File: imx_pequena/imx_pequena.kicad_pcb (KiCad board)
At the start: 2 copper layers, 2 parts, among them U1 MCIMX6Z0DVM09AB, U2 MT41K64M16TW-107:J_TR

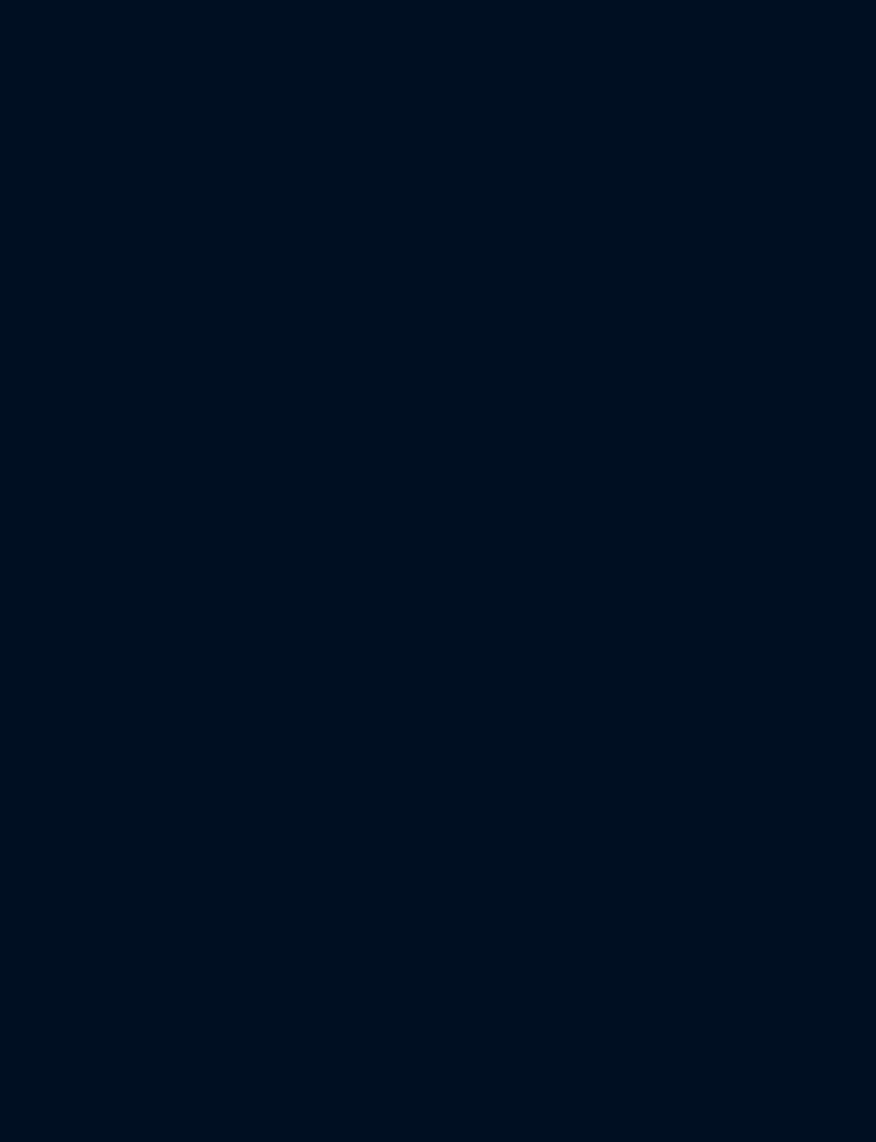
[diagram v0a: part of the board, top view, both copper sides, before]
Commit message: Updated reset pins
Updated reset pins
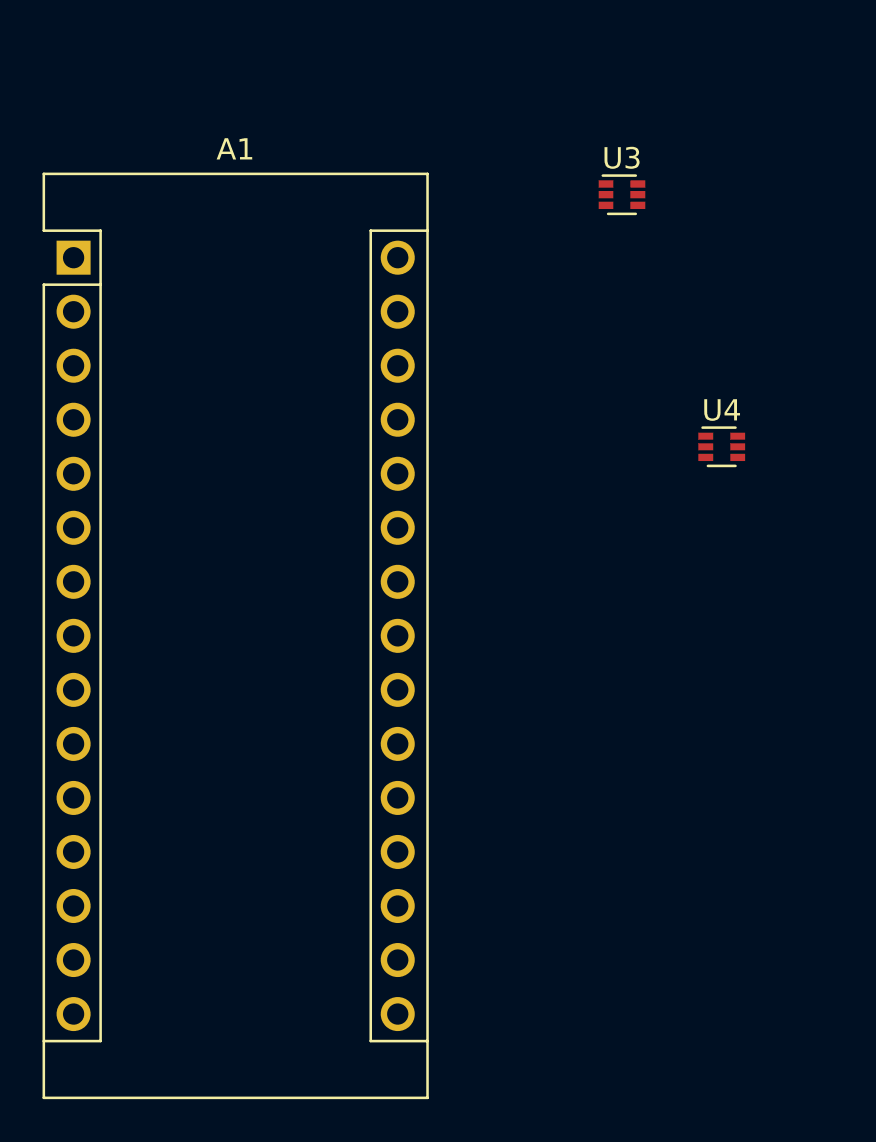
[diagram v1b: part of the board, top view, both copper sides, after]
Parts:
- added A1: Arduino_Nano_Every, Module:Arduino_Nano, F.Cu at (78.8, 100.3)
- added U3: AP62250Z6, Package_TO_SOT_SMD:SOT-563, F.Cu at (104.5, 97.4)
- added U4: AP62250Z6, Package_TO_SOT_SMD:SOT-563, F.Cu at (109.2, 109.2)
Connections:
- U1 pad A2: unconnected-(U1-PadA2) -> /imx_mpu/mpu_f_sd/SD_DATA3
- U1 pad B1: unconnected-(U1-PadB1) -> /imx_mpu/mpu_f_sd/SD_DATA2
- U1 pad B2: unconnected-(U1-PadB2) -> /imx_mpu/mpu_f_sd/SD_DATA1
- U1 pad B3: unconnected-(U1-PadB3) -> /imx_mpu/mpu_f_sd/SD_DATA0
- U1 pad C1: unconnected-(U1-PadC1) -> /imx_mpu/mpu_f_sd/SD_CLK
- U1 pad C2: unconnected-(U1-PadC2) -> /imx_mpu/mpu_f_sd/SD_CMD
- U1 pad C4: unconnected-(U1-PadC4) -> DCDC_3v3
- U1 pad F17: unconnected-(U1-PadF17) -> /imx_mpu/I2C2_SCL
- U1 pad F4: unconnected-(U1-PadF4) -> DCDC_3v3
- U1 pad G13: unconnected-(U1-PadG13) -> /imx_mpu/I2C2_SDA
- U1 pad G2: unconnected-(U1-PadG2) -> Net-(U1-PadG2)
- U1 pad G4: unconnected-(U1-PadG4) -> /imx_mpu/mpu_b_dram/DRAM_RESET
- U1 pad G6: Net-(U1-PadG6) -> Dram_1V35
- U1 pad H1: unconnected-(U1-PadH1) -> /imx_mpu/mpu_b_dram/DRAM_BA1
- U1 pad H13: unconnected-(U1-PadH13) -> Net-(U1-PadH13)
- U1 pad H2: unconnected-(U1-PadH2) -> Net-(U1-PadH2)
- U1 pad H4: unconnected-(U1-PadH4) -> Net-(U1-PadH4)
- U1 pad H6: Net-(U1-PadG6) -> Dram_1V35
- U1 pad J1: unconnected-(U1-PadJ1) -> /imx_mpu/mpu_b_dram/DRAM_WE
- U1 pad J2: unconnected-(U1-PadJ2) -> /imx_mpu/mpu_b_dram/DRAM_CAS
- U1 pad J4: unconnected-(U1-PadJ4) -> Net-(U1-PadJ4)
- U1 pad J6: Net-(U1-PadG6) -> Dram_1V35
- U1 pad K1: unconnected-(U1-PadK1) -> Net-(U1-PadK1)
- U1 pad K2: unconnected-(U1-PadK2) -> /imx_mpu/mpu_b_dram/DRAM_BA2
- U1 pad K3: unconnected-(U1-PadK3) -> Net-(U1-PadK3)
- U1 pad K4: unconnected-(U1-PadK4) -> Net-(U1-PadK4)
- U1 pad K6: Net-(U1-PadG6) -> Dram_1V35
- U1 pad L1: unconnected-(U1-PadL1) -> Net-(U1-PadL1)
- U1 pad L2: unconnected-(U1-PadL2) -> Net-(U1-PadL2)
- U1 pad L4: unconnected-(U1-PadL4) -> Net-(U1-PadL4)
- U1 pad L5: unconnected-(U1-PadL5) -> Net-(U1-PadL5)
- U1 pad L6: Net-(U1-PadG6) -> Dram_1V35
- U1 pad M1: unconnected-(U1-PadM1) -> /imx_mpu/mpu_b_dram/DRAM_BA0
- U1 pad M12: unconnected-(U1-PadM12) -> GND
- U1 pad M14: unconnected-(U1-PadM14) -> /imx_mpu/mpu_a_io/TCK
- U1 pad M2: unconnected-(U1-PadM2) -> Net-(U1-PadM2)
- U1 pad M3: unconnected-(U1-PadM3) -> /imx_mpu/mpu_b_dram/DRAM_CKE
- U1 pad M4: unconnected-(U1-PadM4) -> Net-(U1-PadM4)
- U1 pad M5: unconnected-(U1-PadM5) -> /imx_mpu/mpu_b_dram/DRAM_RAS
- U1 pad M6: Net-(U1-PadG6) -> Dram_1V35
- U1 pad N1: unconnected-(U1-PadN1) -> /imx_mpu/mpu_b_dram/DRAM_ODT
- U1 pad N14: unconnected-(U1-PadN14) -> /imx_mpu/mpu_a_io/JTAG_RESET
- U1 pad N15: unconnected-(U1-PadN15) -> /imx_mpu/mpu_a_io/TDO
- U1 pad N16: unconnected-(U1-PadN16) -> /imx_mpu/mpu_a_io/TDI
- U1 pad N2: unconnected-(U1-PadN2) -> /imx_mpu/mpu_b_dram/DRAM_CS0
- U1 pad N4: unconnected-(U1-PadN4) -> Net-(U1-PadN4)
- U1 pad N6: unconnected-(U1-PadN6) -> VDD_HIGH_CAP
- U1 pad P1: unconnected-(U1-PadP1) -> /imx_mpu/mpu_b_dram/DRAM_SDCLK0_P
- U1 pad P14: unconnected-(U1-PadP14) -> /imx_mpu/mpu_a_io/TMS
- U1 pad P2: unconnected-(U1-PadP2) -> /imx_mpu/mpu_b_dram/DRAM_SDCLK0_N
- U1 pad P4: unconnected-(U1-PadP4) -> /imx_mpu/mpu_b_dram/Dram_vref
- U1 pad P6: unconnected-(U1-PadP6) -> /imx_mpu/mpu_b_dram/DRAM_SDQS0_P
- U1 pad P7: unconnected-(U1-PadP7) -> /imx_mpu/mpu_b_dram/DRAM_SDQS0_N
- U1 pad T1: unconnected-(U1-PadT1) -> /imx_mpu/mpu_b_dram/DRAM_SDQS1_P
- U1 pad T11: unconnected-(U1-PadT11) -> Net-(U1-PadT11)
- U1 pad T12: unconnected-(U1-PadT12) -> /imx_mpu/USB1_VBUS
- U1 pad T13: unconnected-(U1-PadT13) -> /imx_mpu/USB2_DN
- U1 pad T15: unconnected-(U1-PadT15) -> /imx_mpu/USB1_DN
- U1 pad T16: unconnected-(U1-PadT16) -> Net-(U1-PadT16)
- U1 pad T17: unconnected-(U1-PadT17) -> Net-(U1-PadT17)
- U1 pad T2: unconnected-(U1-PadT2) -> /imx_mpu/mpu_b_dram/DRAM_SDQS1_N
- U1 pad T3: unconnected-(U1-PadT3) -> /imx_mpu/mpu_b_dram/DRAM_UDM
- U1 pad T7: unconnected-(U1-PadT7) -> /imx_mpu/mpu_b_dram/DRAM_LDM
- U1 pad U11: unconnected-(U1-PadU11) -> Net-(U1-PadU11)
- U1 pad U12: unconnected-(U1-PadU12) -> /imx_mpu/USB2_VBUS
- U1 pad U13: unconnected-(U1-PadU13) -> /imx_mpu/USB2_DP
- U1 pad U15: unconnected-(U1-PadU15) -> /imx_mpu/USB1_DP
- U1 pad U16: unconnected-(U1-PadU16) -> /imx_mpu/USB1_CHARGE_DETECT
- U2 pad A1: Net-(U2-PadA1) -> Dram_1V35
- U2 pad A8: Net-(U2-PadA1) -> Dram_1V35
- U2 pad A9: Net-(U2-PadA9) -> GND
- U2 pad B1: Net-(U2-PadB1) -> GND
- U2 pad B2: Net-(U2-PadB2) -> Dram_1V35
- U2 pad B3: Net-(U2-PadA9) -> GND
- U2 pad B7: unconnected-(U2-PadB7) -> /imx_mpu/mpu_b_dram/DRAM_SDQS1_N
- U2 pad B9: Net-(U2-PadB1) -> GND
- U2 pad C1: Net-(U2-PadA1) -> Dram_1V35
- U2 pad C7: unconnected-(U2-PadC7) -> /imx_mpu/mpu_b_dram/DRAM_SDQS1_P
- U2 pad C9: Net-(U2-PadA1) -> Dram_1V35
- U2 pad D1: Net-(U2-PadB1) -> GND
- U2 pad D2: Net-(U2-PadA1) -> Dram_1V35
- U2 pad D3: unconnected-(U2-PadD3) -> /imx_mpu/mpu_b_dram/DRAM_UDM
- U2 pad D8: Net-(U2-PadB1) -> GND
- U2 pad D9: Net-(U2-PadB2) -> Dram_1V35
- U2 pad E1: Net-(U2-PadA9) -> GND
- U2 pad E2: Net-(U2-PadB1) -> GND
- U2 pad E7: unconnected-(U2-PadE7) -> /imx_mpu/mpu_b_dram/DRAM_LDM
- U2 pad E8: Net-(U2-PadB1) -> GND
- U2 pad E9: Net-(U2-PadA1) -> Dram_1V35
- U2 pad F1: Net-(U2-PadA1) -> Dram_1V35
- U2 pad F3: unconnected-(U2-PadF3) -> /imx_mpu/mpu_b_dram/DRAM_SDQS0_P
- U2 pad F9: Net-(U2-PadB1) -> GND
- U2 pad G1: Net-(U2-PadB1) -> GND
- U2 pad G3: unconnected-(U2-PadG3) -> /imx_mpu/mpu_b_dram/DRAM_SDQS0_N
- U2 pad G7: Net-(U2-PadB2) -> Dram_1V35
- U2 pad G8: Net-(U2-PadA9) -> GND
- U2 pad G9: Net-(U2-PadB1) -> GND
- U2 pad H1: unconnected-(U2-PadH1) -> /imx_mpu/mpu_b_dram/Dram_vref
- U2 pad H2: Net-(U2-PadA1) -> Dram_1V35
- U2 pad H9: Net-(U2-PadA1) -> Dram_1V35
- U2 pad J2: Net-(U2-PadA9) -> GND
- U2 pad J3: unconnected-(U2-PadJ3) -> /imx_mpu/mpu_b_dram/DRAM_RAS
- U2 pad J7: unconnected-(U2-PadJ7) -> /imx_mpu/mpu_b_dram/DRAM_SDCLK0_P
- U2 pad J8: Net-(U2-PadA9) -> GND
- U2 pad K1: unconnected-(U2-PadK1) -> /imx_mpu/mpu_b_dram/DRAM_ODT
- U2 pad K2: Net-(U2-PadB2) -> Dram_1V35
- U2 pad K3: unconnected-(U2-PadK3) -> /imx_mpu/mpu_b_dram/DRAM_CAS
- U2 pad K7: unconnected-(U2-PadK7) -> /imx_mpu/mpu_b_dram/DRAM_SDCLK0_N
- U2 pad K8: Net-(U2-PadB2) -> Dram_1V35
- U2 pad K9: unconnected-(U2-PadK9) -> /imx_mpu/mpu_b_dram/DRAM_CKE
- U2 pad L2: unconnected-(U2-PadL2) -> /imx_mpu/mpu_b_dram/DRAM_CS0
- U2 pad L3: unconnected-(U2-PadL3) -> /imx_mpu/mpu_b_dram/DRAM_WE
- U2 pad L7: unconnected-(U2-PadL7) -> Net-(U1-PadM4)
- U2 pad L8: unconnected-(U2-PadL8) -> Net-(U2-PadL8)
- U2 pad M1: Net-(U2-PadA9) -> GND
- U2 pad M2: unconnected-(U2-PadM2) -> /imx_mpu/mpu_b_dram/DRAM_BA0
- U2 pad M3: unconnected-(U2-PadM3) -> /imx_mpu/mpu_b_dram/DRAM_BA2
- U2 pad M8: unconnected-(U2-PadM8) -> /imx_mpu/mpu_b_dram/Dram_vref
- U2 pad M9: Net-(U2-PadA9) -> GND
- U2 pad N1: Net-(U2-PadB2) -> Dram_1V35
- U2 pad N2: unconnected-(U2-PadN2) -> Net-(U1-PadM2)
- U2 pad N3: unconnected-(U2-PadN3) -> Net-(U1-PadL5)
- U2 pad N7: unconnected-(U2-PadN7) -> Net-(U1-PadL4)
- U2 pad N8: unconnected-(U2-PadN8) -> /imx_mpu/mpu_b_dram/DRAM_BA1
- U2 pad N9: Net-(U2-PadB2) -> Dram_1V35
- U2 pad P1: Net-(U2-PadA9) -> GND
- U2 pad P2: unconnected-(U2-PadP2) -> Net-(U1-PadL1)
- U2 pad P3: unconnected-(U2-PadP3) -> Net-(U1-PadK1)
- U2 pad P7: unconnected-(U2-PadP7) -> Net-(U1-PadH2)
- U2 pad P8: unconnected-(U2-PadP8) -> Net-(U1-PadK4)
- U2 pad P9: Net-(U2-PadA9) -> GND
- U2 pad R1: Net-(U2-PadB2) -> Dram_1V35
- U2 pad R2: unconnected-(U2-PadR2) -> Net-(U1-PadH4)
- U2 pad R3: unconnected-(U2-PadR3) -> Net-(U1-PadL2)
- U2 pad R7: unconnected-(U2-PadR7) -> Net-(U1-PadK3)
- U2 pad R8: unconnected-(U2-PadR8) -> Net-(U1-PadG2)
- U2 pad R9: Net-(U2-PadB2) -> Dram_1V35
- U2 pad T1: Net-(U2-PadA9) -> GND
- U2 pad T2: unconnected-(U2-PadT2) -> /imx_mpu/mpu_b_dram/DRAM_RESET
- U2 pad T8: unconnected-(U2-PadT8) -> Net-(U1-PadJ4)
- U2 pad T9: Net-(U2-PadA9) -> GND

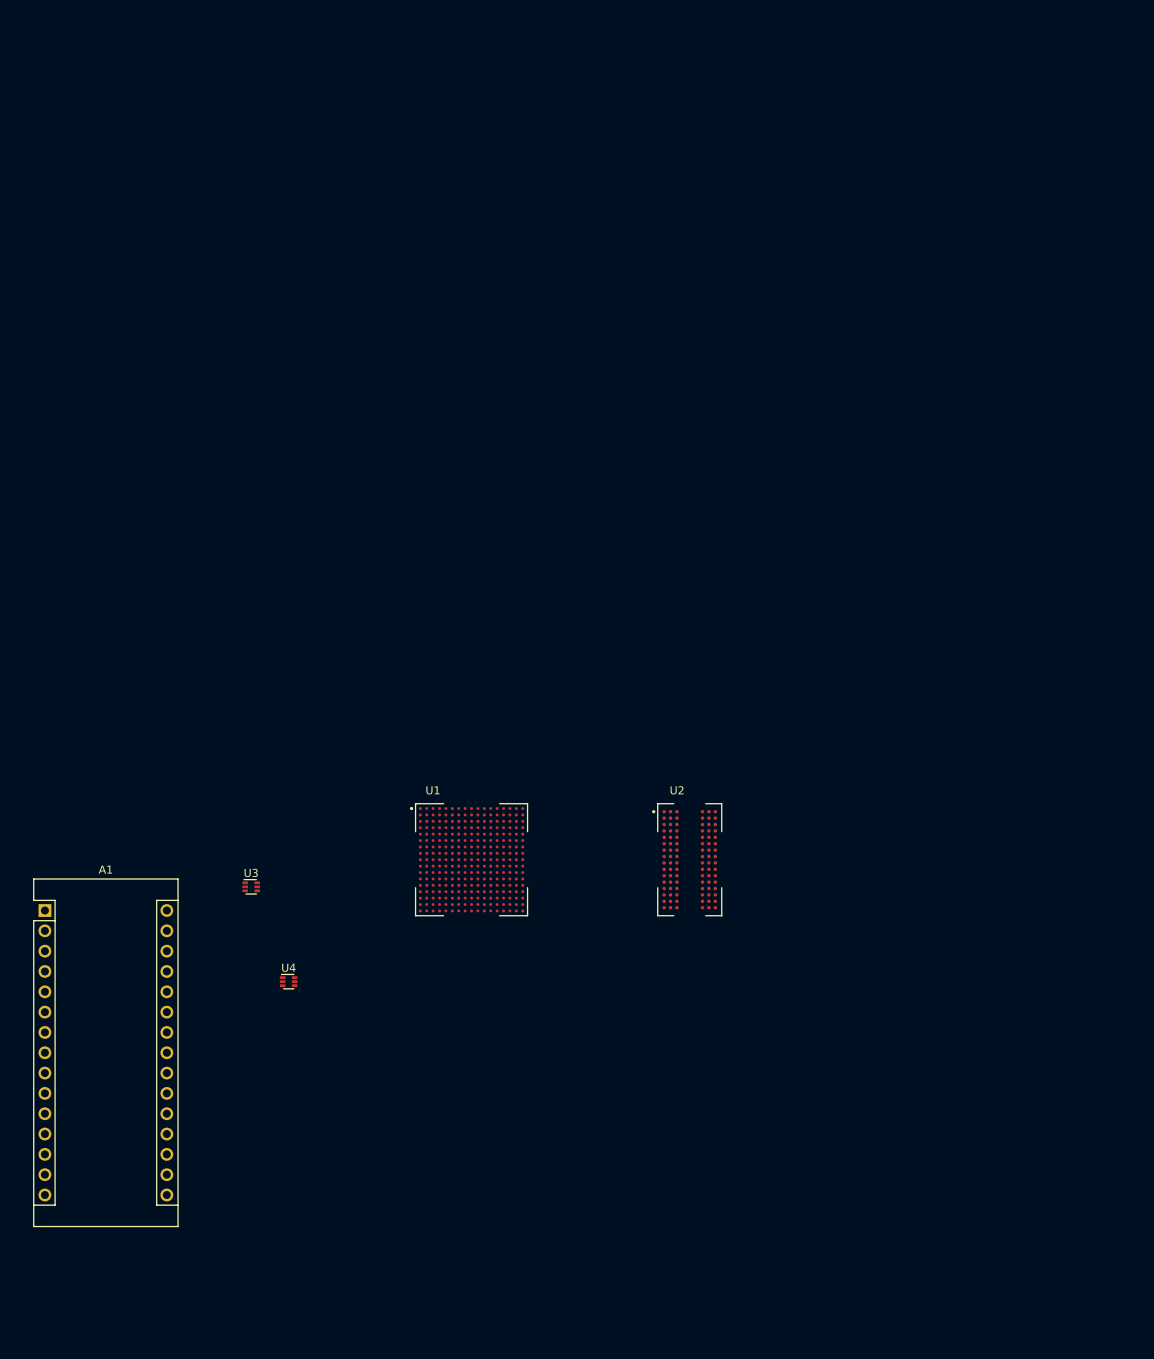
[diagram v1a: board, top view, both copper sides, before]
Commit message: Part Assignment
Assigned GPIOs and assigned footprints to most parts
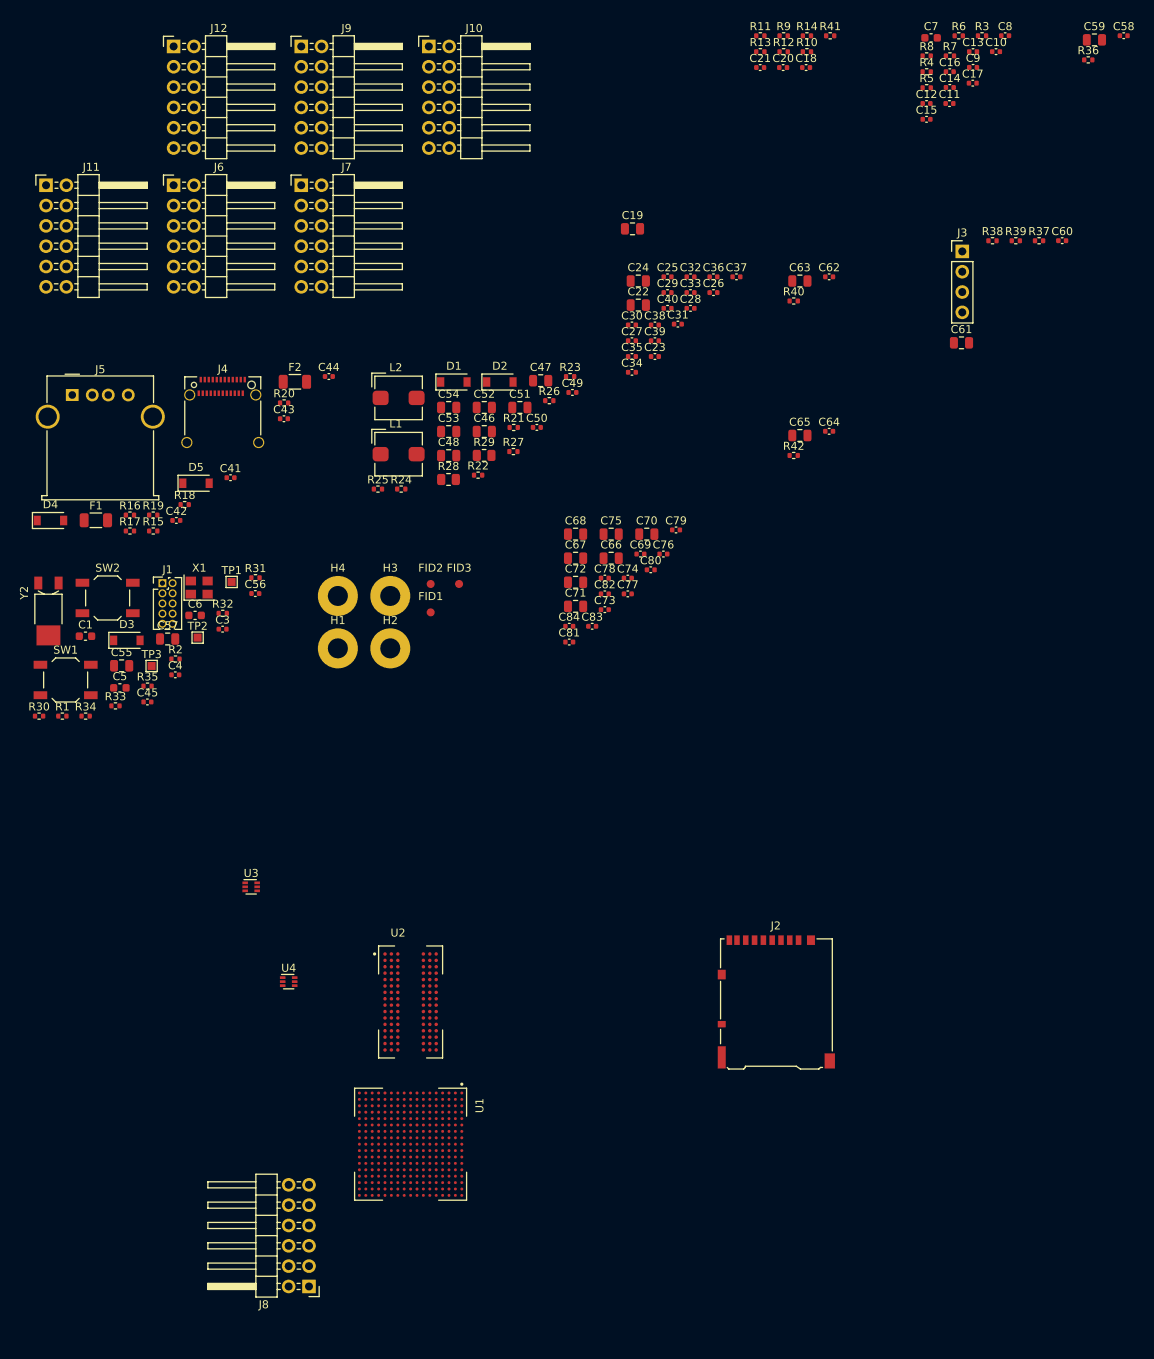
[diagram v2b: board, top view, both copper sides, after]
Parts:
- removed A1: Arduino_Nano_Every, Module:Arduino_Nano
- added C1: 1u, Capacitor_SMD:C_0603_1608Metric, F.Cu at (83.8, 66.0)
- added C10: 0.22u, Capacitor_SMD:C_0402_1005Metric, F.Cu at (197.6, -7.03)
- added C11: 0.22u, Capacitor_SMD:C_0402_1005Metric, F.Cu at (191.8, -0.54)
- added C12: 0.22u, Capacitor_SMD:C_0402_1005Metric, F.Cu at (188.9, -0.54)
- added C13: 0.22u, Capacitor_SMD:C_0402_1005Metric, F.Cu at (194.8, -7.03)
- added C14: DNP, Capacitor_SMD:C_0402_1005Metric, F.Cu at (191.9, -2.55)
- added C15: DNP, Capacitor_SMD:C_0402_1005Metric, F.Cu at (188.9, 1.43)
- added C16: 2.2p, Capacitor_SMD:C_0402_1005Metric, F.Cu at (191.9, -4.52)
- added C17: 2.2p, Capacitor_SMD:C_0402_1005Metric, F.Cu at (194.7, -3.09)
- added C18: 0.1u, Capacitor_SMD:C_0402_1005Metric, F.Cu at (173.9, -5.04)
- added C19: 22u, Capacitor_SMD:C_0805_2012Metric, F.Cu at (152.2, 15.1)
- added C20: 0.22u, Capacitor_SMD:C_0402_1005Metric, F.Cu at (171.0, -5.04)
- added C21: 0.22u, Capacitor_SMD:C_0402_1005Metric, F.Cu at (168.2, -5.04)
- added C22: 22u, Capacitor_SMD:C_0805_2012Metric, F.Cu at (152.9, 24.6)
- added C23: 0.22u, Capacitor_SMD:C_0402_1005Metric, F.Cu at (155.0, 31.1)
- added C24: 10u, Capacitor_SMD:C_0805_2012Metric, F.Cu at (152.9, 21.6)
- added C25: 0.22u, Capacitor_SMD:C_0402_1005Metric, F.Cu at (156.6, 21.1)
- added C26: 0.22u, Capacitor_SMD:C_0402_1005Metric, F.Cu at (162.3, 23.1)
- added C27: 0.22u, Capacitor_SMD:C_0402_1005Metric, F.Cu at (152.1, 29.1)
- added C28: 0.22u, Capacitor_SMD:C_0402_1005Metric, F.Cu at (159.4, 25.1)
- added C29: 0.22u, Capacitor_SMD:C_0402_1005Metric, F.Cu at (156.6, 23.1)
- added C3: 15p, Capacitor_SMD:C_0402_1005Metric, F.Cu at (101.0, 65.2)
- added C30: 0.22u, Capacitor_SMD:C_0402_1005Metric, F.Cu at (152.1, 27.1)
- added C31: 0.22u, Capacitor_SMD:C_0402_1005Metric, F.Cu at (157.9, 27.0)
- added C32: 0.22u, Capacitor_SMD:C_0402_1005Metric, F.Cu at (159.4, 21.1)
- added C33: 0.22u, Capacitor_SMD:C_0402_1005Metric, F.Cu at (159.4, 23.1)
- added C34: 0.22u, Capacitor_SMD:C_0402_1005Metric, F.Cu at (152.1, 33.0)
- added C35: 0.22u, Capacitor_SMD:C_0402_1005Metric, F.Cu at (152.1, 31.1)
- added C36: 0.22u, Capacitor_SMD:C_0402_1005Metric, F.Cu at (162.3, 21.1)
- added C37: 0.22u, Capacitor_SMD:C_0402_1005Metric, F.Cu at (165.2, 21.1)
- added C38: 0.22u, Capacitor_SMD:C_0402_1005Metric, F.Cu at (155.0, 27.1)
- added C39: 0.22u, Capacitor_SMD:C_0402_1005Metric, F.Cu at (155.0, 29.1)
- added C4: 15p, Capacitor_SMD:C_0402_1005Metric, F.Cu at (95.0, 70.9)
- added C40: 0.22u, Capacitor_SMD:C_0402_1005Metric, F.Cu at (156.6, 25.1)
- added C41: 47pF, Capacitor_SMD:C_0402_1005Metric, F.Cu at (102.0, 46.2)
- added C42: 47pF, Capacitor_SMD:C_0402_1005Metric, F.Cu at (95.2, 51.6)
- added C43: 47pF, Capacitor_SMD:C_0402_1005Metric, F.Cu at (108.6, 38.9)
- added C44: 47pF, Capacitor_SMD:C_0402_1005Metric, F.Cu at (114.2, 33.6)
- added C45: DNP, Capacitor_SMD:C_0402_1005Metric, F.Cu at (91.6, 74.3)
- added C46: 10u, Capacitor_SMD:C_0805_2012Metric, F.Cu at (133.7, 40.5)
- added C47: 10u, Capacitor_SMD:C_0805_2012Metric, F.Cu at (140.7, 34.1)
- added C48: 10n, Capacitor_SMD:C_0805_2012Metric, F.Cu at (129.2, 43.5)
- added C49: 100n, Capacitor_SMD:C_0402_1005Metric, F.Cu at (144.7, 35.6)
- added C5: 1u, Capacitor_SMD:C_0603_1608Metric, F.Cu at (88.1, 72.5)
- added C50: 100n, Capacitor_SMD:C_0402_1005Metric, F.Cu at (140.2, 39.9)
- added C51: 22u, Capacitor_SMD:C_0805_2012Metric, F.Cu at (138.1, 37.5)
- added C52: 22u, Capacitor_SMD:C_0805_2012Metric, F.Cu at (133.7, 37.5)
- added C53: 22u, Capacitor_SMD:C_0805_2012Metric, F.Cu at (129.2, 40.5)
- added C54: 22u, Capacitor_SMD:C_0805_2012Metric, F.Cu at (129.2, 37.5)
- added C55: DNP, Capacitor_SMD:C_0805_2012Metric, F.Cu at (88.3, 69.7)
- added C56: 0.22uF, Capacitor_SMD:C_0402_1005Metric, F.Cu at (105.0, 60.7)
- added C57: 10u, Capacitor_SMD:C_0805_2012Metric, F.Cu at (94.1, 66.4)
- added C58: 0.22uF, Capacitor_SMD:C_0402_1005Metric, F.Cu at (213.6, -9.02)
- added C59: 10u, Capacitor_SMD:C_0805_2012Metric, F.Cu at (209.9, -8.50)
- added C6: 1u, Capacitor_SMD:C_0603_1608Metric, F.Cu at (97.5, 63.4)
- added C60: 0.22uF, Capacitor_SMD:C_0402_1005Metric, F.Cu at (205.9, 16.6)
- added C61: 10u, Capacitor_SMD:C_0805_2012Metric, F.Cu at (193.3, 29.4)
- added C62: 0.22uF, Capacitor_SMD:C_0402_1005Metric, F.Cu at (176.8, 21.1)
- added C63: 10u, Capacitor_SMD:C_0805_2012Metric, F.Cu at (173.1, 21.6)
- added C64: 0.22uF, Capacitor_SMD:C_0402_1005Metric, F.Cu at (176.8, 40.4)
- added C65: 10u, Capacitor_SMD:C_0805_2012Metric, F.Cu at (173.1, 41.0)
- added C66: 22u, Capacitor_SMD:C_0805_2012Metric, F.Cu at (149.5, 56.3)
- added C67: 22u, Capacitor_SMD:C_0805_2012Metric, F.Cu at (145.1, 56.3)
- added C68: 4.7u, Capacitor_SMD:C_0805_2012Metric, F.Cu at (145.1, 53.3)
- added C69: 0.22u, Capacitor_SMD:C_0402_1005Metric, F.Cu at (153.2, 55.8)
- added C7: 4.7u, Capacitor_SMD:C_0603_1608Metric, F.Cu at (189.5, -8.75)
- added C70: 22u, Capacitor_SMD:C_0805_2012Metric, F.Cu at (154.0, 53.3)
- added C71: 22u, Capacitor_SMD:C_0805_2012Metric, F.Cu at (145.1, 62.3)
- added C72: 10u, Capacitor_SMD:C_0805_2012Metric, F.Cu at (145.1, 59.3)
- added C73: 0.22u, Capacitor_SMD:C_0402_1005Metric, F.Cu at (148.7, 62.7)
- added C74: 0.22u, Capacitor_SMD:C_0402_1005Metric, F.Cu at (151.6, 58.8)
- added C75: 4.7u, Capacitor_SMD:C_0805_2012Metric, F.Cu at (149.5, 53.3)
- added C76: 0.22u, Capacitor_SMD:C_0402_1005Metric, F.Cu at (156.1, 55.8)
- added C77: 0.22u, Capacitor_SMD:C_0402_1005Metric, F.Cu at (151.6, 60.8)
- added C78: 0.22u, Capacitor_SMD:C_0402_1005Metric, F.Cu at (148.7, 58.8)
- added C79: 0.22u, Capacitor_SMD:C_0402_1005Metric, F.Cu at (157.6, 52.8)
- added C8: 0.1u, Capacitor_SMD:C_0402_1005Metric, F.Cu at (198.8, -9.02)
- added C80: 0.22u, Capacitor_SMD:C_0402_1005Metric, F.Cu at (154.5, 57.7)
- added C81: 0.22u, Capacitor_SMD:C_0402_1005Metric, F.Cu at (144.3, 66.8)
- added C82: 0.22u, Capacitor_SMD:C_0402_1005Metric, F.Cu at (148.7, 60.8)
- added C83: 0.22u, Capacitor_SMD:C_0402_1005Metric, F.Cu at (147.2, 64.8)
- added C84: 0.22u, Capacitor_SMD:C_0402_1005Metric, F.Cu at (144.3, 64.8)
- added C9: 0.1u, Capacitor_SMD:C_0402_1005Metric, F.Cu at (194.8, -5.06)
- added D1: D_Zener, Diode_SMD:D_SOD-123, F.Cu at (129.9, 34.3)
- added D2: D_Schottky, Diode_SMD:D_SOD-123, F.Cu at (135.6, 34.3)
- added D3: D_Schottky, Diode_SMD:D_SOD-123, F.Cu at (89.0, 66.6)
- added D4: D_TVS, Diode_SMD:D_SOD-123, F.Cu at (79.4, 51.6)
- added D5: D_TVS, Diode_SMD:D_SOD-123, F.Cu at (97.6, 46.9)
- added F1: Fuse_Small, Resistor_SMD:R_1206_3216Metric, F.Cu at (85.1, 51.5)
- added F2: Fuse_Small, Resistor_SMD:R_1206_3216Metric, F.Cu at (110.0, 34.2)
- added FID1: Fiducial, Fiducial:Fiducial_1mm_Mask2mm, F.Cu at (127.0, 63.1)
- added FID2: Fiducial, Fiducial:Fiducial_1mm_Mask2mm, F.Cu at (127.0, 59.5)
- added FID3: Fiducial, Fiducial:Fiducial_1mm_Mask2mm, F.Cu at (130.5, 59.5)
- added H1: MountingHole, MountingHole:MountingHole_2.5mm_Pad, F.Cu at (115.4, 67.6)
- added H2: MountingHole, MountingHole:MountingHole_2.5mm_Pad, F.Cu at (121.9, 67.6)
- added H3: MountingHole, MountingHole:MountingHole_2.5mm_Pad, F.Cu at (121.9, 61.0)
- added H4: MountingHole_Pad, MountingHole:MountingHole_2.5mm_Pad, F.Cu at (115.4, 61.0)
- added J1: Conn_ARM_JTAG_SWD_10, Connector_PinHeader_1.27mm:PinHeader_2x05_P1.27mm_Vertical, F.Cu at (93.4, 59.4)
- added J10: Conn_02x06_Top_Bottom, Connector_PinHeader_2.54mm:PinHeader_2x06_P2.54mm_Horizontal, F.Cu at (126.7, -7.68)
- added J11: Conn_02x06_Top_Bottom, Connector_PinHeader_2.54mm:PinHeader_2x06_P2.54mm_Horizontal, F.Cu at (78.9, 9.67)
- added J12: Conn_02x06_Top_Bottom, Connector_PinHeader_2.54mm:PinHeader_2x06_P2.54mm_Horizontal, F.Cu at (94.8, -7.68)
- added J2: Micro_SD_Card, Connector_Card:microSD_HC_Hirose_DM3AT-SF-PEJM5, F.Cu at (170.2, 111.8)
- added J3: Conn_01x04, Connector_PinHeader_2.54mm:PinHeader_1x04_P2.54mm_Vertical, F.Cu at (193.4, 17.9)
- added J4: USB_C_Receptacle, Connector_USB:USB_C_Receptacle_Amphenol_12401610E4-2A_CircularHoles, F.Cu at (101.0, 39.0)
- added J5: USB_A, Connector_USB:USB_A_Molex_67643_Horizontal, F.Cu at (82.2, 35.9)
- added J6: Conn_02x06_Top_Bottom, Connector_PinHeader_2.54mm:PinHeader_2x06_P2.54mm_Horizontal, F.Cu at (94.8, 9.67)
- added J7: Conn_02x06_Top_Bottom, Connector_PinHeader_2.54mm:PinHeader_2x06_P2.54mm_Horizontal, F.Cu at (110.8, 9.67)
- added J8: Conn_02x06_Top_Bottom, Connector_PinHeader_2.54mm:PinHeader_2x06_P2.54mm_Horizontal, F.Cu at (111.8, 147.3)
- added J9: Conn_02x06_Top_Bottom, Connector_PinHeader_2.54mm:PinHeader_2x06_P2.54mm_Horizontal, F.Cu at (110.8, -7.68)
- added L1: 2.2u, Inductor_SMD:L_Bourns_SRP5030T, F.Cu at (123.0, 43.3)
- added L2: 1.0u, Inductor_SMD:L_Bourns_SRP5030T, F.Cu at (123.0, 36.3)
- added R1: 4.7K, Resistor_SMD:R_0402_1005Metric, F.Cu at (80.9, 76.0)
- added R10: 10K, Resistor_SMD:R_0402_1005Metric, F.Cu at (174.0, -7.02)
- added R11: 10K, Resistor_SMD:R_0402_1005Metric, F.Cu at (168.2, -9.01)
- added R12: 10K, Resistor_SMD:R_0402_1005Metric, F.Cu at (171.1, -7.02)
- added R13: 10K, Resistor_SMD:R_0402_1005Metric, F.Cu at (168.2, -7.02)
- added R14: 10K, Resistor_SMD:R_0402_1005Metric, F.Cu at (174.0, -9.01)
- added R15: 22, Resistor_SMD:R_0402_1005Metric, F.Cu at (92.3, 52.9)
- added R16: 22, Resistor_SMD:R_0402_1005Metric, F.Cu at (89.4, 50.9)
- added R17: 5.1K, Resistor_SMD:R_0402_1005Metric, F.Cu at (89.4, 52.9)
- added R18: 5.1K, Resistor_SMD:R_0402_1005Metric, F.Cu at (96.2, 49.6)
- added R19: 22, Resistor_SMD:R_0402_1005Metric, F.Cu at (92.3, 50.9)
- added R2: 4.7K, Resistor_SMD:R_0402_1005Metric, F.Cu at (95.1, 68.9)
- added R20: 22, Resistor_SMD:R_0402_1005Metric, F.Cu at (108.7, 36.9)
- added R21: 10K, Resistor_SMD:R_0402_1005Metric, F.Cu at (137.3, 40.0)
- added R22: 10K, Resistor_SMD:R_0402_1005Metric, F.Cu at (132.9, 45.9)
- added R23: 31.6K, Resistor_SMD:R_0402_1005Metric, F.Cu at (144.4, 33.6)
- added R24: 10K, Resistor_SMD:R_0402_1005Metric, F.Cu at (123.3, 47.6)
- added R25: 75, Resistor_SMD:R_0402_1005Metric, F.Cu at (120.4, 47.6)
- added R26: 6.8K, Resistor_SMD:R_0402_1005Metric, F.Cu at (141.8, 36.6)
- added R27: 10K, Resistor_SMD:R_0402_1005Metric, F.Cu at (137.3, 43.0)
- added R28: 0.1, Resistor_SMD:R_0805_2012Metric, F.Cu at (129.2, 46.5)
- added R29: 0.1, Resistor_SMD:R_0805_2012Metric, F.Cu at (133.7, 43.4)
- added R3: 1.5K, Resistor_SMD:R_0402_1005Metric, F.Cu at (195.9, -9.01)
- added R30: 10K, Resistor_SMD:R_0402_1005Metric, F.Cu at (78.0, 76.0)
- added R31: 10K, Resistor_SMD:R_0402_1005Metric, F.Cu at (105.1, 58.7)
- added R32: DNI, Resistor_SMD:R_0402_1005Metric, F.Cu at (101.0, 63.2)
- added R33: 0, Resistor_SMD:R_0402_1005Metric, F.Cu at (87.6, 74.8)
- added R34: 0, Resistor_SMD:R_0402_1005Metric, F.Cu at (83.8, 76.0)
- added R35: DNP, Resistor_SMD:R_0402_1005Metric, F.Cu at (91.6, 72.3)
- added R36: 0, Resistor_SMD:R_0402_1005Metric, F.Cu at (209.2, -6.00)
- added R37: 4.7K, Resistor_SMD:R_0402_1005Metric, F.Cu at (203.0, 16.6)
- added R38: 4.7K, Resistor_SMD:R_0402_1005Metric, F.Cu at (197.2, 16.6)
- added R39: 0, Resistor_SMD:R_0402_1005Metric, F.Cu at (200.1, 16.6)
- added R4: 1.5K, Resistor_SMD:R_0402_1005Metric, F.Cu at (189.0, -4.51)
- added R40: 0, Resistor_SMD:R_0402_1005Metric, F.Cu at (172.3, 24.1)
- added R41: 0, Resistor_SMD:R_0402_1005Metric, F.Cu at (176.9, -9.01)
- added R42: 0, Resistor_SMD:R_0402_1005Metric, F.Cu at (172.3, 43.5)
- added R5: 240, Resistor_SMD:R_0402_1005Metric, F.Cu at (189.0, -2.52)
- added R6: 10K, Resistor_SMD:R_0402_1005Metric, F.Cu at (193.0, -9.01)
- added R7: 240, Resistor_SMD:R_0402_1005Metric, F.Cu at (191.9, -6.50)
- added R8: 470, Resistor_SMD:R_0402_1005Metric, F.Cu at (189.0, -6.50)
- added R9: 10K, Resistor_SMD:R_0402_1005Metric, F.Cu at (171.1, -9.01)
- added SW1: SW_SPST, Button_Switch_SMD:SW_SPST_TL3342, F.Cu at (81.3, 71.5)
- added SW2: SW_SPST, Button_Switch_SMD:SW_SPST_TL3342, F.Cu at (86.6, 61.3)
- added TP1: Bootmode 0, TestPoint:TestPoint_Pad_1.0x1.0mm, F.Cu at (102.1, 59.3)
- added TP2: Bootmode 1, TestPoint:TestPoint_Pad_1.0x1.0mm, F.Cu at (97.8, 66.2)
- added TP3: SNVS, TestPoint:TestPoint_Pad_1.0x1.0mm, F.Cu at (92.1, 69.8)
- added X1: ASE-xxxMHz, Oscillator:Oscillator_SMD_Abracon_ASE-4Pin_3.2x2.5mm, F.Cu at (98.0, 60.0)
- added Y2: Crystal, Crystal:Crystal_SMD_MicroCrystal_MS1V-T1K, F.Cu at (79.2, 62.9)
- moved U2 39.2 mm to (124.5, 111.8)
- moved U1 36.4 mm to (124.5, 129.5), turned to -90 degrees
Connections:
- net DCDC_3v3 renamed /imx_mpu/mpu_f_sd/SD_3v3
- net Net-(U1-PadG10) renamed /imx_mpu/mpu_h_power/ARM_CAP
- net Net-(U1-PadG8) renamed /imx_mpu/mpu_h_power/SOC_CAP
- net Net-(U1-PadR14) renamed /imx_mpu/mpu_h_power/HIGH_CAP
- U1 pad A1: Net-(U1-PadA1) -> GND
- U1 pad A10: unconnected-(U1-PadA10) -> ecspi_ss2
- U1 pad A11: unconnected-(U1-PadA11) -> GPIO3_14
- U1 pad A12: unconnected-(U1-PadA12) -> GPIO3_19
- U1 pad A13: unconnected-(U1-PadA13) -> GPIO3_23
- U1 pad A14: unconnected-(U1-PadA14) -> ecspi_mosi
- U1 pad A17: Net-(U1-PadA1) -> GND
- U1 pad A8: unconnected-(U1-PadA8) -> GPIO3_0
- U1 pad A9: unconnected-(U1-PadA9) -> GPIO3_6
- U1 pad B10: unconnected-(U1-PadB10) -> ecspi_ss1
- U1 pad B11: unconnected-(U1-PadB11) -> GPIO3_13
- U1 pad B12: unconnected-(U1-PadB12) -> GPIO3_18
- U1 pad B13: unconnected-(U1-PadB13) -> GPIO3_22
- U1 pad B14: unconnected-(U1-PadB14) -> ecspi_ss0
- U1 pad B16: unconnected-(U1-PadB16) -> ecspi_miso
- U1 pad B8: unconnected-(U1-PadB8) -> GPIO3_1
- U1 pad B9: unconnected-(U1-PadB9) -> GPIO3_5
- U1 pad C10: unconnected-(U1-PadC10) -> GPIO3_9
- U1 pad C11: Net-(U1-PadA1) -> GND
- U1 pad C12: unconnected-(U1-PadC12) -> ecspi_rdy
- U1 pad C13: unconnected-(U1-PadC13) -> GPIO3_21
- U1 pad C14: unconnected-(U1-PadC14) -> ecspi_sclk
- U1 pad C15: Net-(U1-PadA1) -> GND
- U1 pad C3: Net-(U1-PadA1) -> GND
- U1 pad C7: Net-(U1-PadA1) -> GND
- U1 pad C9: unconnected-(U1-PadC9) -> GPIO3_3
- U1 pad D10: unconnected-(U1-PadD10) -> GPIO3_8
- U1 pad D11: unconnected-(U1-PadD11) -> ecspi_ss3
- U1 pad D12: unconnected-(U1-PadD12) -> GPIO3_16
- U1 pad D13: unconnected-(U1-PadD13) -> GPIO3_20
- U1 pad D14: unconnected-(U1-PadD14) -> GPIO3_24
- U1 pad D9: unconnected-(U1-PadD9) -> GPIO3_2
- U1 pad E10: unconnected-(U1-PadE10) -> PWM3_out
- U1 pad E11: Net-(U1-PadA1) -> GND
- U1 pad E12: unconnected-(U1-PadE12) -> GPIO3_15
- U1 pad E13: unconnected-(U1-PadE13) -> Net-(U1-PadE13)
- U1 pad E7: unconnected-(U1-PadE7) -> Net-(U1-PadE7)
- U1 pad E8: Net-(U1-PadA1) -> GND
- U1 pad E9: unconnected-(U1-PadE9) -> GPIO3_4
- U1 pad F10: Net-(U1-PadF10) -> GND
- U1 pad F11: Net-(U1-PadF10) -> GND
- U1 pad F12: Net-(U1-PadF10) -> GND
- U1 pad F13: unconnected-(U1-PadF13) -> Net-(U1-PadF13)
- U1 pad F6: Net-(U1-PadA1) -> GND
- U1 pad F7: Net-(U1-PadA1) -> GND
- U1 pad F8: Net-(U1-PadF10) -> GND
- U1 pad F9: Net-(U1-PadF10) -> GND
- U1 pad G12: Net-(U1-PadF10) -> GND
- U1 pad G15: Net-(U1-PadF10) -> GND
- U1 pad G16: unconnected-(U1-PadG16) -> /imx_mpu/I2C1_SDA
- U1 pad G17: unconnected-(U1-PadG17) -> /imx_mpu/I2C1_SCL
- U1 pad G3: Net-(U1-PadF10) -> GND
- U1 pad G5: Net-(U1-PadF10) -> GND
- U1 pad G7: Net-(U1-PadF10) -> GND
- U1 pad H10: Net-(U1-PadH10) -> 3v3
- U1 pad H12: Net-(U1-PadH12) -> GND
- U1 pad H14: unconnected-(U1-PadH14) -> /imx_mpu/UART2_RTS
- U1 pad H16: unconnected-(U1-PadH16) -> /imx_mpu/UART3_RX
- U1 pad H17: unconnected-(U1-PadH17) -> /imx_mpu/UART3_TX
- U1 pad H7: Net-(U1-PadH12) -> GND
- U1 pad H9: Net-(U1-PadH10) -> 3v3
- U1 pad J10: Net-(U1-PadH10) -> 3v3
- U1 pad J12: Net-(U1-PadH12) -> GND
- U1 pad J13: unconnected-(U1-PadJ13) -> Net-(U1-PadE13)
- U1 pad J14: unconnected-(U1-PadJ14) -> /imx_mpu/UART1_CTS
- U1 pad J15: unconnected-(U1-PadJ15) -> /imx_mpu/UART2_CTS
- U1 pad J16: unconnected-(U1-PadJ16) -> /imx_mpu/UART2_RX
- U1 pad J17: unconnected-(U1-PadJ17) -> /imx_mpu/UART2_TX
- U1 pad J5: Net-(U1-PadH12) -> GND
- U1 pad J7: Net-(U1-PadH12) -> GND
- U1 pad J9: Net-(U1-PadH10) -> 3v3
- U1 pad K10: Net-(U1-PadH10) -> 3v3
- U1 pad K12: Net-(U1-PadH12) -> GND
- U1 pad K13: unconnected-(U1-PadK13) -> GPIO1_0
- U1 pad K14: unconnected-(U1-PadK14) -> /imx_mpu/UART1_TX
- U1 pad K15: unconnected-(U1-PadK15) -> /imx_mpu/UART1_RTS
- U1 pad K16: unconnected-(U1-PadK16) -> /imx_mpu/UART1_RX
- U1 pad K17: unconnected-(U1-PadK17) -> GPIO1_6
- U1 pad K7: Net-(U1-PadH12) -> GND
- U1 pad K9: Net-(U1-PadH10) -> 3v3
- U1 pad L12: Net-(U1-PadH12) -> GND
- U1 pad L13: Net-(U1-PadL13) -> 3v3
- U1 pad L14: unconnected-(U1-PadL14) -> GPIO1_2
- U1 pad L15: unconnected-(U1-PadL15) -> GPIO1_1
- U1 pad L16: unconnected-(U1-PadL16) -> GPIO1_7
- U1 pad L17: unconnected-(U1-PadL17) -> GPIO1_3
- U1 pad L3: Net-(U1-PadH12) -> GND
- U1 pad L7: Net-(U1-PadH12) -> GND
- U1 pad M10: Net-(U1-PadM10) -> GND
- U1 pad M11: Net-(U1-PadM10) -> GND
- U1 pad M13: Net-(U1-PadL13) -> 3v3
- U1 pad M15: unconnected-(U1-PadM15) -> PWM2_out
- U1 pad M16: unconnected-(U1-PadM16) -> GPIO1_4
- U1 pad M17: unconnected-(U1-PadM17) -> PWM4_out
- U1 pad M7: Net-(U1-PadM10) -> GND
- U1 pad M8: Net-(U1-PadM10) -> GND
- U1 pad M9: Net-(U1-PadM10) -> GND
- U1 pad N12: unconnected-(U1-PadN12) -> /imx_mpu/mpu_h_power/SNVS_CAP
- U1 pad N13: Net-(U1-PadL13) -> 3v3
- U1 pad N17: unconnected-(U1-PadN17) -> PWM1_out
- U1 pad N3: Net-(U1-PadM10) -> GND
- U1 pad N5: Net-(U1-PadM10) -> GND
- U1 pad N7: unconnected-(U1-PadN7) -> GND
- U1 pad P12: unconnected-(U1-PadP12) -> 3v3
- U1 pad P13: unconnected-(U1-PadP13) -> Net-(U1-PadP13)
- U1 pad P15: unconnected-(U1-PadP15) -> Net-(U1-PadP15)
- U1 pad P8: unconnected-(U1-PadP8) -> /imx_mpu/mpu_a_io/~{Reset}
- U1 pad R11: Net-(U1-PadR11) -> GND
- U1 pad R12: unconnected-(U1-PadR12) -> /imx_mpu/mpu_h_power/USB_CAP
- U1 pad R16: Net-(U1-PadR11) -> GND
- U1 pad R17: Net-(U1-PadR11) -> GND
- U1 pad R3: Net-(U1-PadM10) -> GND
- U1 pad R5: Net-(U1-PadM10) -> GND
- U1 pad R7: Net-(U1-PadM10) -> GND
- U1 pad R8: unconnected-(U1-PadR8) -> /imx_mpu/mpu_a_io/~{ONOFF}
- U1 pad T10: unconnected-(U1-PadT10) -> Net-(U1-PadT10)
- U1 pad T14: Net-(U1-PadR11) -> GND
- U1 pad T16: Net-(U1-PadT16) -> unconnected-(U1-PadT16)
- U1 pad T9: unconnected-(U1-PadT9) -> Net-(U1-PadT9)
- U1 pad U1: Net-(U1-PadR11) -> GND
- U1 pad U10: unconnected-(U1-PadU10) -> Net-(U1-PadU10)
- U1 pad U14: Net-(U1-PadR11) -> GND
- U1 pad U17: Net-(U1-PadR11) -> GND
- U3 pad 1: Net-(C46-Pad1) -> USB_5V
